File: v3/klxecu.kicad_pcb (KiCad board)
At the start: 4 copper layers, 80.3 x 86.4 mm, 131 parts, among them IC1 SP721, J1 cam_sensor, J2 Conn_01x06, J3 DIP8, J4 Conn_02x04_Counter_Clockwise, J5 TACH_OUT, J6 IGN_ARD_OUT, J7 IGN_DRV_OUT, J8 IGN_CONN, Q1 SSM3K357R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

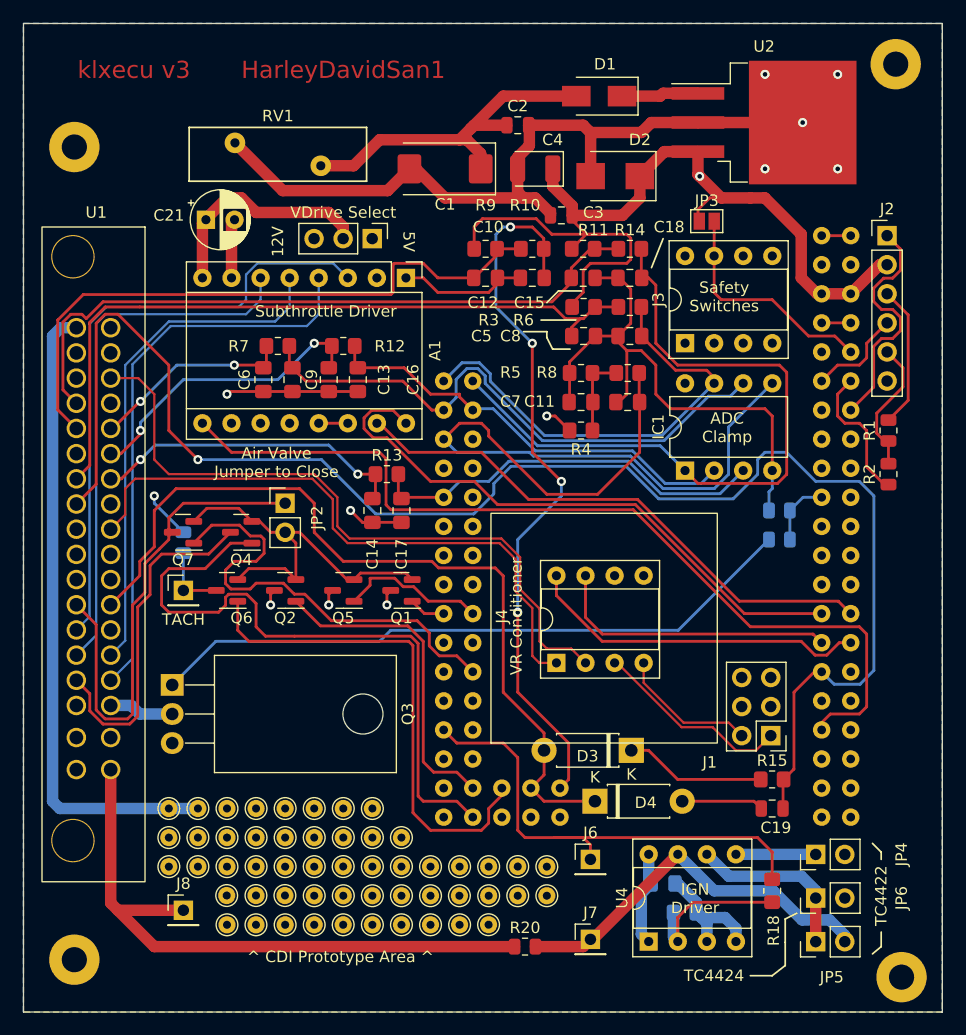
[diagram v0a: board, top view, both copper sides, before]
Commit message: Delete gerber files, make a few updates to v3
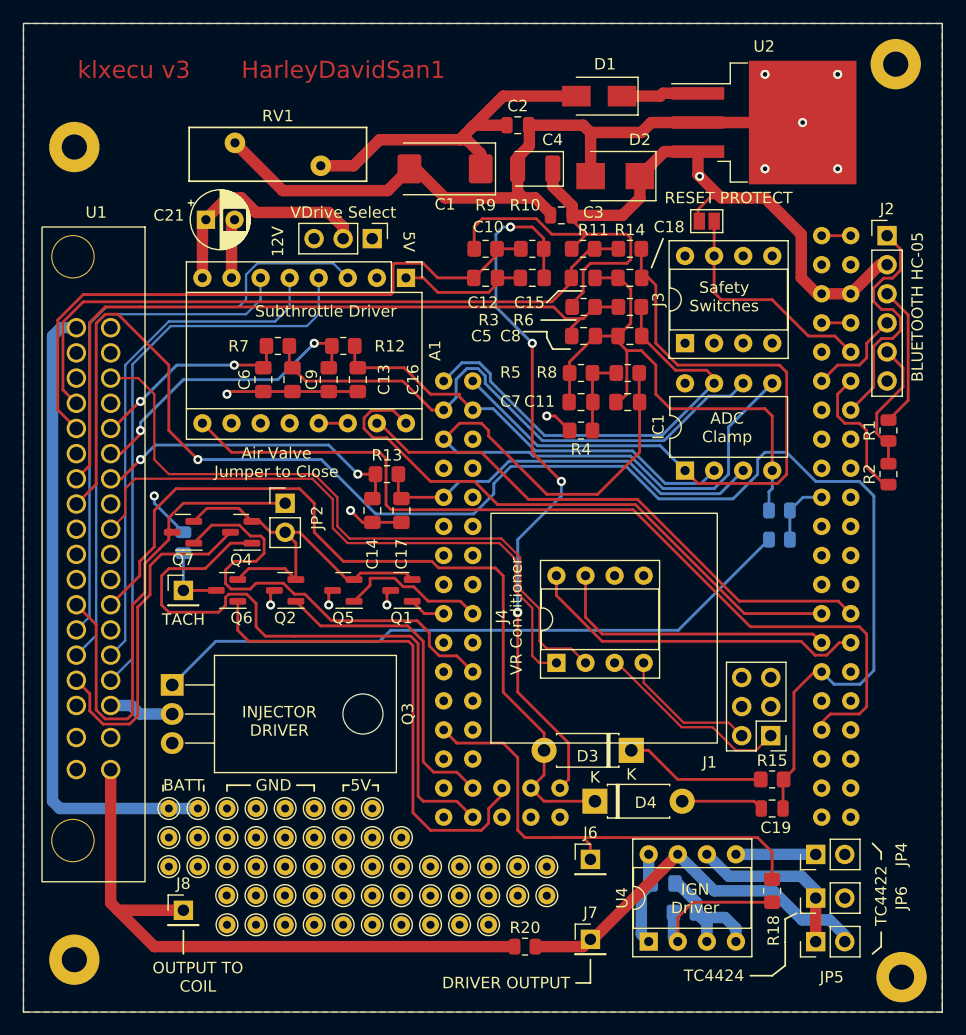
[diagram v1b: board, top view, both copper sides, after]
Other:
- board text added: "BATT"
- board text added: "BLUETOOTH HC-05"
- board text added: "DRIVER OUTPUT"
- board text added: "GND"
- board text added: "INJECTOR DRIVER"
- board text added: "OUTPUT TO COIL"
- board text added: "RESET PROTECT"
- board text removed: "^ CDI Prototype Area ^"
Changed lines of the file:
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@@
     (property "Sheetname" "Sensors & Inputs")
     (attr exclude_from_pos_files)
-    (fp_text reference "JP3" (at 0 -1.8) (layer "F.SilkS")
+    (fp_text reference "JP3" (at 0 -1.8) (layer "F.SilkS") hide
       (effects (font (size 1 1) (thickness 0.15)))
     )
@@
       (net 105 "unconnected-(U3-PadVIN)") (pintype "passive+no_connect"))
   )
+  (gr_line (start 53.34 99.568) (end 53.34 100.076) (layer "F.SilkS") (width 0.15))
   (gr_line (start 100.33 105.41) (end 99.568 104.648) (layer "F.SilkS") (width 0.15))
   (gr_line (start 73.66 58.928) (end 70.612 58.928) (layer "F.SilkS") (width 0.15))
   (gr_line (start 81.28 51.816) (end 80.264 54.356) (layer "F.SilkS") (width 0.15))
   (gr_line (start 74.168 56.388) (end 72.136 56.388) (layer "F.SilkS") (width 0.15))
+  (gr_line (start 43.18 99.568) (end 43.18 100.076) (layer "F.SilkS") (width 0.15))
   (gr_line (start 91.948 113.284) (end 91.948 111.252) (layer "F.SilkS") (width 0.15))
   (gr_line (start 90.805 116.205) (end 91.948 115.316) (layer "F.SilkS") (width 0.15))
+  (gr_line (start 49.276 99.568) (end 50.8 99.568) (layer "F.SilkS") (width 0.15))
   (gr_line (start 100.33 105.41) (end 100.33 106.045) (layer "F.SilkS") (width 0.15))
+  (gr_line (start 39.37 112.268) (end 39.37 114.3) (layer "F.SilkS") (width 0.15))
   (gr_line (start 71.12 59.944) (end 69.088 59.944) (layer "F.SilkS") (width 0.15))
+  (gr_line (start 53.34 99.568) (end 53.848 99.568) (layer "F.SilkS") (width 0.15))
+  (gr_line (start 74.93 114.808) (end 74.93 116.84) (layer "F.SilkS") (width 0.15))
   (gr_line (start 100.33 113.665) (end 100.33 112.395) (layer "F.SilkS") (width 0.15))
   (gr_line (start 100.33 113.665) (end 99.568 114.3) (layer "F.SilkS") (width 0.15))
+  (gr_line (start 74.93 116.84) (end 73.66 116.84) (layer "F.SilkS") (width 0.15))
   (gr_line (start 90.805 116.205) (end 88.9 116.205) (layer "F.SilkS") (width 0.15))
   (gr_line (start 91.948 111.252) (end 92.964 110.744) (layer "F.SilkS") (width 0.15))
   (gr_line (start 71.628 61.468) (end 71.12 60.452) (layer "F.SilkS") (width 0.15))
+  (gr_line (start 41.148 99.568) (end 41.148 100.076) (layer "F.SilkS") (width 0.15))
+  (gr_line (start 55.88 99.568) (end 56.388 99.568) (layer "F.SilkS") (width 0.15))
+  (gr_line (start 50.8 99.568) (end 50.8 100.076) (layer "F.SilkS") (width 0.15))
+  (gr_line (start 45.212 99.568) (end 43.18 99.568) (layer "F.SilkS") (width 0.15))
+  (gr_line (start 56.388 99.568) (end 56.388 100.076) (layer "F.SilkS") (width 0.15))
   (gr_line (start 71.12 60.452) (end 71.12 59.944) (layer "F.SilkS") (width 0.15))
   (gr_line (start 72.136 56.388) (end 71.12 57.404) (layer "F.SilkS") (width 0.15))
+  (gr_line (start 37.592 99.568) (end 37.592 100.076) (layer "F.SilkS") (width 0.15))
   (gr_line (start 73.152 61.468) (end 71.628 61.468) (layer "F.SilkS") (width 0.15))
   (gr_line (start 91.948 115.316) (end 91.948 113.284) (layer "F.SilkS") (width 0.15))
@@
     (effects (font (size 1 1) (thickness 0.15)))
   )
-  (gr_text "^ CDI Prototype Area ^" (at 53.086 114.554) (layer "F.SilkS")
-    (effects (font (size 1 1) (thickness 0.15)))
-  )
   (gr_text "Air Valve\nJumper to Close" (at 47.498 71.374) (layer "F.SilkS")
     (effects (font (size 1 1) (thickness 0.15)))
@@
     (effects (font (size 1 1) (thickness 0.15)))
   )
+  (gr_text "5V" (at 54.864 99.568) (layer "F.SilkS")
+    (effects (font (size 1 1) (thickness 0.15)))
+  )
   (gr_text "12V" (at 47.625 52.07 90) (layer "F.SilkS")
     (effects (font (size 1 1) (thickness 0.15)))
   )
+  (gr_text "GND" (at 47.244 99.568) (layer "F.SilkS")
+    (effects (font (size 1 1) (thickness 0.15)))
+  )
   (gr_text "ADC\nClamp" (at 86.868 68.326) (layer "F.SilkS")
     (effects (font (size 1 1) (thickness 0.15)))
   )
+  (gr_text "BLUETOOTH HC-05" (at 103.505 57.785 90) (layer "F.SilkS")
+    (effects (font (size 1 1) (thickness 0.15)))
+  )
+  (gr_text "BATT" (at 39.37 99.568) (layer "F.SilkS")
+    (effects (font (size 1 1) (thickness 0.15)))
+  )
+  (gr_text "DRIVER OUTPUT" (at 67.564 116.84) (layer "F.SilkS")
+    (effects (font (size 1 1) (thickness 0.15)))
+  )
+  (gr_text "RESET PROTECT" (at 86.995 48.26) (layer "F.SilkS")
+    (effects (font (size 1 1) (thickness 0.15)))
+  )
   (gr_text "IGN\nDriver" (at 84.074 109.474) (layer "F.SilkS")
     (effects (font (size 1 1) (thickness 0.15)))
@@
     (effects (font (size 1 1) (thickness 0.15)))
   )
+  (gr_text "OUTPUT TO\nCOIL" (at 40.64 116.332) (layer "F.SilkS")
+    (effects (font (size 1 1) (thickness 0.15)))
+  )
   (gr_text "TACH" (at 39.37 85.09) (layer "F.SilkS")
     (effects (font (size 1 1) (thickness 0.15)))
   )
+  (gr_text "INJECTOR\nDRIVER" (at 47.752 93.98) (layer "F.SilkS")
+    (effects (font (size 1 1) (thickness 0.15)))
+  )
   (gr_text "TC4424" (at 85.725 116.205) (layer "F.SilkS")
     (effects (font (size 1 1) (thickness 0.15)))
@@
   (segment (start 39.37 64.135) (end 47.625 64.135) (width 0.25) (layer "B.Cu") (net 17))
   (segment (start 35.6245 68.58) (end 35.6245 67.8805) (width 0.25) (layer "B.Cu") (net 17))
-  (segment (start 30.506499 58.425489) (end 29.533501 58.425489) (width 0.25) (layer "F.Cu") (net 18))
   (segment (start 77.375 52.705) (end 75.295 52.705) (width 0.25) (layer "F.Cu") (net 18))
+  (segment (start 71.56952 57.33548) (end 30.623511 57.33548) (width 0.25) (layer "F.Cu") (net 18))
+  (segment (start 73.2575 55.6475) (end 71.56952 57.33548) (width 0.25) (layer "F.Cu") (net 18))
+  (segment (start 30.623511 57.33548) (end 28.845489 59.113501) (width 0.25) (layer "F.Cu") (net 18))
   (segment (start 28.845489 59.113501) (end 28.845489 65.025489) (width 0.25) (layer "F.Cu") (net 18))
-  (segment (start 28.845489 65.025489) (end 30.02 66.2) (width 0.25) (layer "F.Cu") (net 18))
   (segment (start 73.2575 54.3775) (end 73.2575 55.245) (width 0.25) (layer "F.Cu") (net 18))
   (segment (start 74.93 52.705) (end 73.2575 54.3775) (width 0.25) (layer "F.Cu") (net 18))
-  (segment (start 73.2575 55.6475) (end 71.56952 57.33548) (width 0.25) (layer "F.Cu") (net 18))
-  (segment (start 30.884283 58.803273) (end 30.506499 58.425489) (width 0.25) (layer "F.Cu") (net 18))
-  (segment (start 71.56952 57.33548) (end 32.352076 57.33548) (width 0.25) (layer "F.Cu") (net 18))
-  (segment (start 75.295 52.705) (end 74.93 52.705) (width 0.25) (layer "F.Cu") (net 18))
-  (segment (start 29.533501 58.425489) (end 28.845489 59.113501) (width 0.25) (layer "F.Cu") (net 18))
-  (segment (start 32.352076 57.33548) (end 30.884283 58.803273) (width 0.25) (layer "F.Cu") (net 18))
   (segment (start 73.2575 55.245) (end 73.2575 55.6475) (width 0.25) (layer "F.Cu") (net 18))
+  (segment (start 28.845489 65.025489) (end 30.02 66.2) (width 0.25) (layer "F.Cu") (net 18))
+  (segment (start 75.295 52.705) (end 74.93 52.705) (width 0.25) (layer "F.Cu") (net 18))
   (segment (start 54.34 62.8275) (end 54.61 63.0975) (width 0.25) (layer "F.Cu") (net 19))
   (segment (start 54.34 61.1925) (end 54.34 62.8275) (width 0.25) (layer "F.Cu") (net 19))
@@
     (connect_pads (clearance 0.508))
     (min_thickness 0.254) (filled_areas_thickness no)
-    (fill yes (mode hatch) (thermal_gap 0.508) (thermal_bridge_width 0.508) (smoothing chamfer) (radius 1)
-      (hatch_thickness 0.5) (hatch_gap 0.5) (hatch_orientation 45)
-      (hatch_border_algorithm hatch_thickness) (hatch_min_hole_area 0.3))
+    (fill yes (thermal_gap 0.508) (thermal_bridge_width 0.508) (smoothing chamfer) (radius 1))
     (polygon
       (pts
@@
     (connect_pads (clearance 0.508))
     (min_thickness 0.254) (filled_areas_thickness no)
-    (fill yes (mode hatch) (thermal_gap 0.508) (thermal_bridge_width 0.508) (smoothing chamfer) (radius 1)
-      (hatch_thickness 0.5) (hatch_gap 0.5) (hatch_orientation 45)
-      (hatch_border_algorithm hatch_thickness) (hatch_min_hole_area 0.3))
+    (fill yes (thermal_gap 0.508) (thermal_bridge_width 0.508) (smoothing chamfer) (radius 1))
     (polygon
       (pts

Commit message: Reposition components to improve routing and resolve warnings
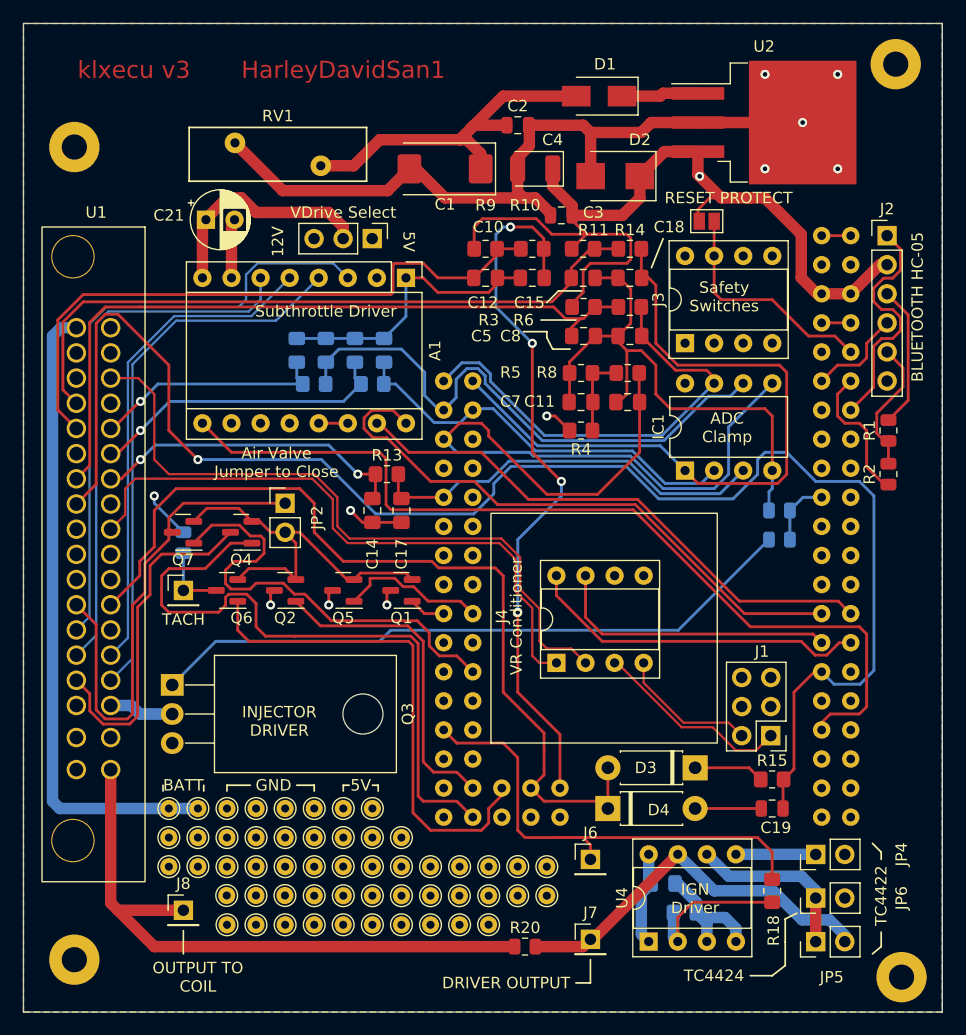
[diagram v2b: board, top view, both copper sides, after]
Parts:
- C13, C16, C6, C9, R12, R7: moved to B.Cu
- moved D3 5.78 mm to (84.1, 98.0)
- moved R7 4.60 mm to (50.8, 64.5)
- moved R12 4.18 mm to (55.9, 64.5)
- moved C6 3.89 mm to (49.3, 61.6), turned to 90 degrees
- moved C9 3.89 mm to (51.8, 61.6), turned to 90 degrees
- moved C13 3.43 mm to (54.4, 61.6), turned to 90 degrees
- moved C16 3.43 mm to (56.9, 61.6), turned to 90 degrees
- moved D4 1.30 mm to (76.5, 101.6)
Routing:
- net +5V: track 102.0 -> 95.5 mm
- net CLUTCH-SW: track 72.3 -> 75.8 mm
- net TPS: track 17.7 -> 20.5 mm, vias 2 -> 1
- net MAP-ARD-A3: track 38.0 -> 35.8 mm
- net SUB-A+: track 49.7 -> 47.8 mm
- net SUB-B+: track 44.9 -> 43.4 mm
- net GND: track 213.6 -> 214.4 mm, vias 7 -> 6
- net TPS-ARD-A2: track 50.4 -> 49.7 mm
- net SELF-DIAG-ARD-D53: track 62.8 -> 62.2 mm
- net MAP: track 26.0 -> 26.5 mm, vias 2 -> 1

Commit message: Move o2s resistors to back of board
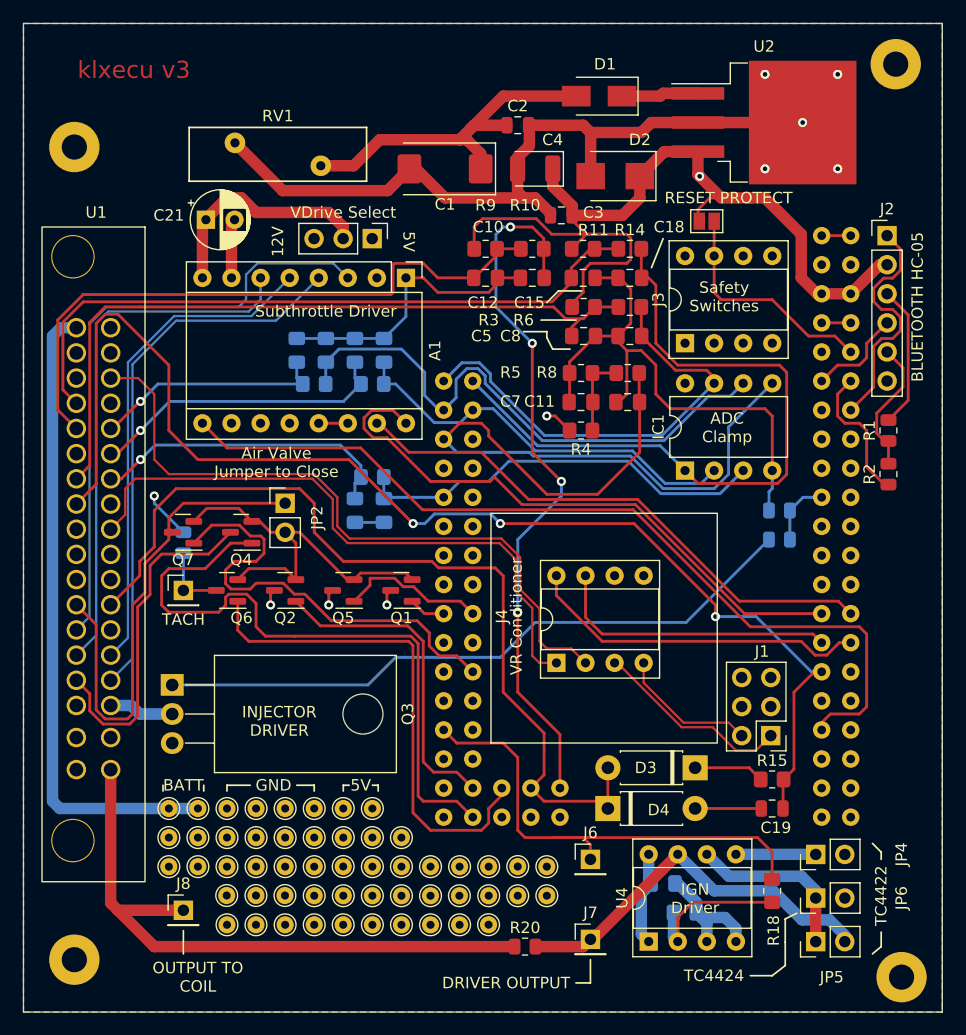
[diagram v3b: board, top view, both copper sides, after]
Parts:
- C14, C17, R13: moved to B.Cu
- moved C14 1.52 mm to (54.4, 75.6)
- moved C17 1.52 mm to (56.9, 75.6)
- moved R13 1.30 mm to (55.9, 72.6)
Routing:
- net VSS: track 137.3 -> 111.5 mm, vias 1 -> 3
- net EN-ARD-D24: track 79.5 -> 77.2 mm
- net GND: track 214.4 -> 212.0 mm, vias 6 -> 5
- net O2S-ARD-A8: track 35.5 -> 36.6 mm
- net O2S: track 27.7 -> 26.9 mm, vias 2 -> 1
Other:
- board text removed: "HarleyDavidSan1"
